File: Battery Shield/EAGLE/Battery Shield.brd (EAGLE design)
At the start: 58.5 x 15.7 mm, 30 parts, among them IC1 MCP73871, U1 TPS61200

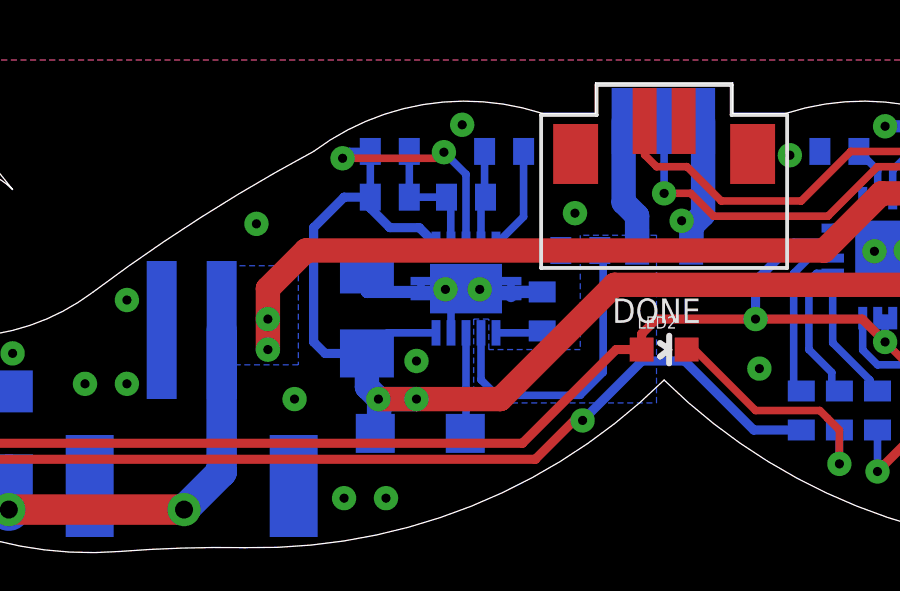
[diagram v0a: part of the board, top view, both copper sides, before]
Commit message: connected the DGND and GND nets manually on the PCB
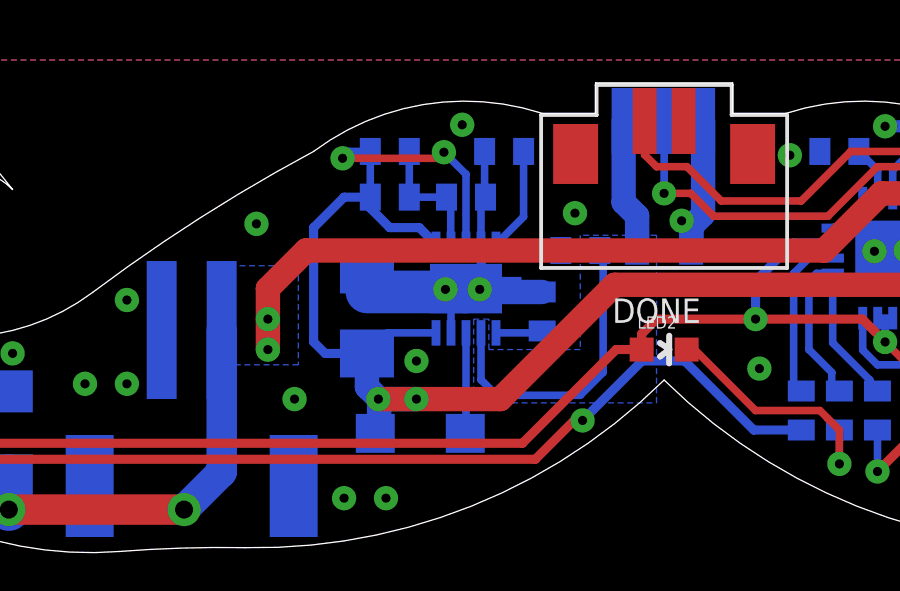
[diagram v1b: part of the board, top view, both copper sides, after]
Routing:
- net GND: track 29.3 -> 27.9 mm
- net N$18: track 0.00 -> 1.02 mm
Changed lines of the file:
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@@
 <wire x1="38.87" y1="8.64" x2="38.87" y2="8.374" width="0.254" layer="16"/>
 <wire x1="40.87" y1="8.778" x2="39.37" y2="8.778" width="0.254" layer="16"/>
-<wire x1="39.37" y1="8.778" x2="39.37" y2="8.89" width="0.254" layer="16"/>
 <wire x1="47.274" y1="14.478" x2="47.274" y2="11.3584" width="0.8128" layer="16"/>
 <wire x1="47.274" y1="11.3584" x2="46.8884" y2="10.9728" width="0.8128" layer="16"/>
@@
 <wire x1="55.626" y1="13.97" x2="55.626" y2="13.574" width="0.4064" layer="16"/>
 <wire x1="55.626" y1="13.574" x2="55.514" y2="13.462" width="0.4064" layer="16"/>
-<wire x1="41.91" y1="8.778" x2="36.068" y2="8.778" width="0.4064" layer="16"/>
 <wire x1="36.068" y1="8.778" x2="36.068" y2="9.528" width="0.4064" layer="16"/>
-<wire x1="41.91" y1="8.778" x2="40.87" y2="8.778" width="0.4064" layer="16"/>
 <wire x1="40.87" y1="8.778" x2="40.87" y2="8.64" width="0.4064" layer="16"/>
+<wire x1="36.068" y1="8.778" x2="39.37" y2="8.778" width="1.4224" layer="16"/>
+<wire x1="39.37" y1="8.778" x2="39.37" y2="8.89" width="1.4224" layer="16"/>
+<wire x1="41.91" y1="8.778" x2="39.8272" y2="8.778" width="0.8128" layer="16"/>
+<wire x1="39.8272" y1="8.778" x2="39.8272" y2="8.8646" width="0.8128" layer="16"/>
 </signal>
 <signal name="VBATT_OUT">
@@
 <via x="36.449" y="5.207" extent="1-16" drill="0.3048" diameter="0.6096"/>
 </signal>
+<signal name="N$18">
+<wire x1="39.878" y1="9.398" x2="39.878" y2="10.414" width="0.3048" layer="16"/>
+</signal>
 </signals>

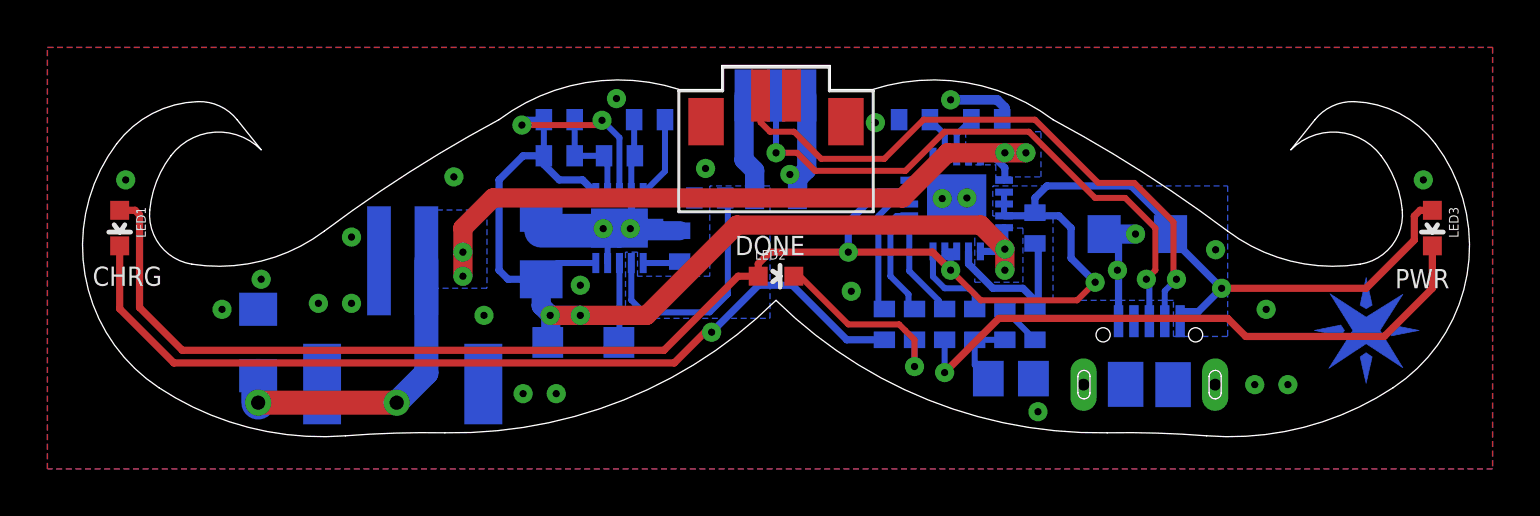
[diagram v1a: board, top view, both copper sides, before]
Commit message: updated shield BOMs and boards
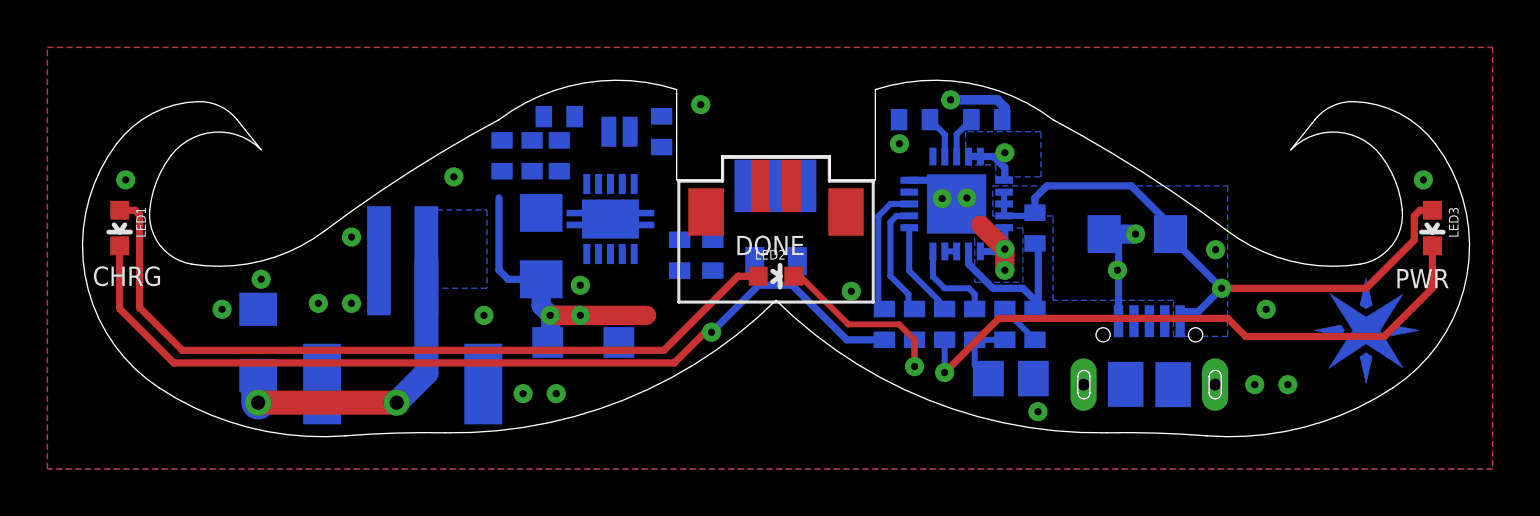
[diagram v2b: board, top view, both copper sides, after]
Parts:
- added R5: 10K, SparkFun-Passives:0402-RES
- added SJ1: SOLDERJUMPERNO, SparkFun-Passives:SJ_2S-NO
- moved U$1 3.81 mm to (46.0, 10.7)
- moved R4 3.03 mm to (36.8, 13.6)
- moved C4 2.79 mm to (46.0, 7.49)
- moved R1 2.42 mm to (43.3, 7.75), turned to 270 degrees
- moved C2 2.41 mm to (34.4, 11.9), turned to 90 degrees
- moved R3 1.90 mm to (35.7, 11.9), turned to 270 degrees
- moved R2 0.72 mm to (41.1, 13.0), turned to 270 degrees
- moved U1 0.54 mm to (39.0, 9.27)
- moved C1 0.38 mm to (41.9, 7.75)
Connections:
- new net N$19: R5.1, SJ1.2, U1.8
- net GND: now also SJ1.1
- net VBATT_OUT: now also R5.2; no longer U1.8
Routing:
- net VBATT_OUT: track 51.6 -> 17.8 mm, vias 5 -> 3
- net VBUS: track 87.5 -> 60.2 mm, vias 4 -> 1
- net N$5: track 42.8 -> 15.8 mm, vias 6 -> 3
- net D-: track 26.1 -> 0.00 mm, vias 1 -> 0
- net D+: track 25.2 -> 0.00 mm, vias 2 -> 0
- net GND: track 27.9 -> 11.8 mm, vias 29 -> 25
- net +5V: track 16.0 -> 0.00 mm
- net N$4: track 5.72 -> 0.00 mm
- net N$3: track 4.40 -> 0.00 mm
- net N$1: track 3.36 -> 0.03 mm
- net DGND: track 3.17 -> 0.00 mm
- net N$2: track 1.60 -> 0.00 mm
- net N$18: track 1.02 -> 0.00 mm
- removed copper zone on layer 16, net +5V
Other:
- board size 58.5 x 15.7 mm -> 58.5 x 15 mm

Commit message: updated changes to the battery shield
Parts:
- removed THERMISTOR: 10k, rcl:R0805
- added R6: 10K, SparkFun-Passives:0402-RES
- moved R5 2.95 mm to (33.9, 11.7)
- moved R4 2.60 mm to (39.3, 14.5)
- moved U$2 2.56 mm to (68.3, 4.22)
- moved LED2 1.68 mm to (46.0, 5.18)
- moved C2 0.64 mm to (35.0, 11.7)
- moved R3 0.50 mm to (36.1, 11.7)
- moved SJ1 0.29 mm to (39.2, 12.8)
- moved R2 0.07 mm to (41.1, 12.9)
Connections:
- net GND: now also R6.1; no longer THERMISTOR.2
- net N$7: now also R6.2; no longer THERMISTOR.1
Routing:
- net VBUS: track 60.2 -> 108.9 mm, vias 1 -> 5
- net N$5: track 15.8 -> 45.8 mm, vias 3 -> 6
- net D-: track 0.00 -> 29.4 mm, vias 0 -> 1
- net D+: track 0.00 -> 29.3 mm, vias 0 -> 2
- net VBATT_OUT: track 17.8 -> 41.2 mm
- net GND: track 11.8 -> 30.7 mm, vias 25 -> 26
- net +5V: track 0.00 -> 12.1 mm
- net N$3: track 0.00 -> 8.82 mm
- net N$19: track 0.00 -> 7.97 mm, vias 0 -> 2
- net N$4: track 0.00 -> 6.62 mm
- net DGND: track 0.00 -> 5.41 mm
- net N$1: track 0.03 -> 3.91 mm
- net N$2: track 0.00 -> 2.21 mm
- net N$18: track 0.00 -> 1.02 mm
- net N$8: track 38.2 -> 39.0 mm
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- added copper zone on layer 16, net +5V
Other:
- board size 58.5 x 15 mm -> 58.5 x 15.2 mm

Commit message: updated battery shield
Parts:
- JP2: value USB_MALE -> USBFCI
- renumbered U$1 to JP2
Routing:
- net GND: track 30.7 -> 45.3 mm
- net VBUS: track 108.9 -> 104.4 mm
- net D-: track 29.4 -> 27.7 mm
- net D+: track 29.3 -> 27.6 mm
- net N$8: track 39.0 -> 37.4 mm
- net VBATT_OUT: track 41.2 -> 40.1 mm
- net N$16: track 25.7 -> 24.7 mm
- net N$10: track 7.76 -> 7.10 mm
- net +5V: track 12.1 -> 11.6 mm
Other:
- board text added: "+"
